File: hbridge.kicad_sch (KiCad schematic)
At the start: 25 parts, among them J11 Conn_01x06_Male, J12 Screw_Terminal_01x04, J21 Conn_01x03_Male, Q1 2N7000, Q11 2N7000, Q13 2N3904, Q14 2N3906, Q15 2N3904, Q16 2N3906, Q17 STP20NF06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

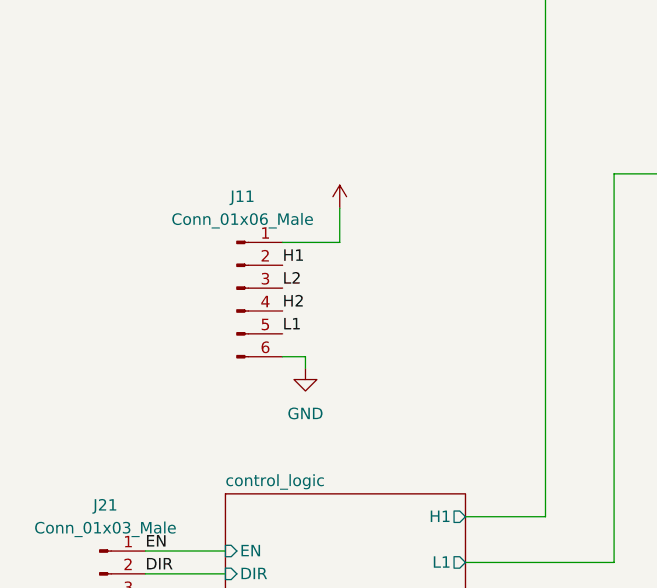
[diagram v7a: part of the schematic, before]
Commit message: Used internal layer to show redlines
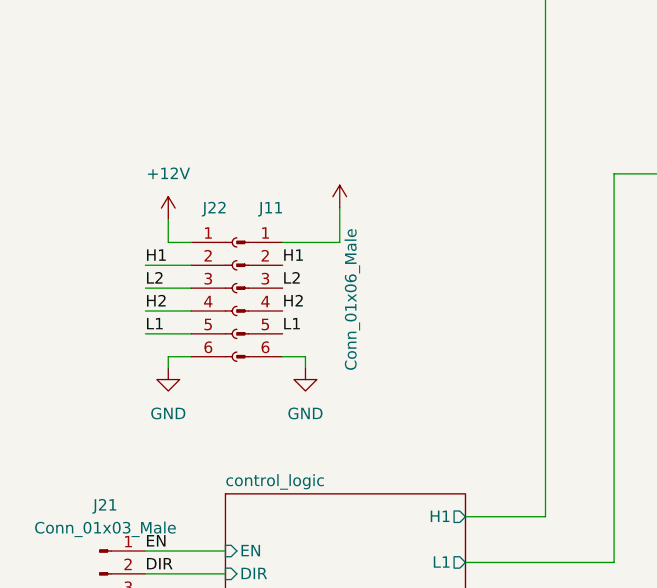
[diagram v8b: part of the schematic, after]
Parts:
- added J22: (no value), symbol Connector:Conn_01x06_Female
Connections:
- net +12V: now also J22.1 (Pin_1)
- net GND: now also J22.6 (Pin_6)
- net H1: now also J22.2 (Pin_2)
- net H2: now also J22.4 (Pin_4)
- net L1: now also J22.5 (Pin_5)
- net L2: now also J22.3 (Pin_3)
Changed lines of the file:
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@@
+    (stroke (width 0) (type default) (color 0 0 0 0))
+  )
+  (wire (pts (xy 35.56 105.41) (xy 38.1 105.41))
     (stroke (width 0) (type default) (color 0 0 0 0))
   )
@@
     (stroke (width 0) (type default) (color 0 0 0 0))
   )
+  (wire (pts (xy 33.02 100.33) (xy 38.1 100.33))
+    (stroke (width 0) (type default) (color 0 0 0 0))
+  )
   (wire (pts (xy 81.28 138.43) (xy 86.36 138.43))
     (stroke (width 0) (type default) (color 0 0 0 0))
@@
     (stroke (width 0) (type default) (color 0 0 0 0))
   )
+  (wire (pts (xy 35.56 106.68) (xy 35.56 105.41))
+    (stroke (width 0) (type default) (color 0 0 0 0))
+  )
   (wire (pts (xy 138.43 39.37) (xy 138.43 48.26))
     (stroke (width 0) (type default) (color 0 0 0 0))
@@
     (stroke (width 0) (type default) (color 0 0 0 0))
   )
+  (wire (pts (xy 35.56 92.71) (xy 38.1 92.71))
+    (stroke (width 0) (type default) (color 0 0 0 0))
+  )
   (wire (pts (xy 125.73 124.46) (xy 125.73 142.24))
     (stroke (width 0) (type default) (color 0 0 0 0))
@@
     (stroke (width 0) (type default) (color 0 0 0 0))
   )
+  (wire (pts (xy 33.02 97.79) (xy 38.1 97.79))
+    (stroke (width 0) (type default) (color 0 0 0 0))
+  )
   (wire (pts (xy 114.3 115.57) (xy 114.3 121.92))
     (stroke (width 0) (type default) (color 0 0 0 0))
@@
     (stroke (width 0) (type default) (color 0 0 0 0))
   )
+  (wire (pts (xy 35.56 90.17) (xy 35.56 92.71))
+    (stroke (width 0) (type default) (color 0 0 0 0))
+  )
   (wire (pts (xy 181.61 125.73) (xy 190.5 125.73))
     (stroke (width 0) (type default) (color 0 0 0 0))
@@
     (stroke (width 0) (type default) (color 0 0 0 0))
   )
+  (wire (pts (xy 33.02 102.87) (xy 38.1 102.87))
+    (stroke (width 0) (type default) (color 0 0 0 0))
+  )
   (wire (pts (xy 96.52 36.83) (xy 92.71 36.83))
     (stroke (width 0) (type default) (color 0 0 0 0))
@@
   )
   (wire (pts (xy 114.3 36.83) (xy 114.3 43.18))
+    (stroke (width 0) (type default) (color 0 0 0 0))
+  )
+  (wire (pts (xy 33.02 95.25) (xy 38.1 95.25))
     (stroke (width 0) (type default) (color 0 0 0 0))
   )
@@
     (effects (font (size 1.27 1.27)) (justify left bottom))
   )
+  (label "L1" (at 33.02 102.87 0)
+    (effects (font (size 1.27 1.27)) (justify left bottom))
+  )
   (label "OUT1" (at 153.67 63.5 0)
     (effects (font (size 1.27 1.27)) (justify left bottom))
   )
+  (label "L2" (at 33.02 97.79 0)
+    (effects (font (size 1.27 1.27)) (justify left bottom))
+  )
   (label "boot1" (at 116.84 36.83 0)
     (effects (font (size 1.27 1.27)) (justify left bottom))
@@
     (effects (font (size 1.27 1.27)) (justify left bottom))
   )
+  (label "H1" (at 33.02 95.25 0)
+    (effects (font (size 1.27 1.27)) (justify left bottom))
+  )
+  (label "H2" (at 33.02 100.33 0)
+    (effects (font (size 1.27 1.27)) (justify left bottom))
+  )
   (label "DIR" (at 33.02 129.54 0)
     (effects (font (size 1.27 1.27)) (justify left bottom))
@@
     )
     (property "Datasheet" "" (id 3) (at 92.71 114.3 0)
+      (effects (font (size 1.27 1.27)) hide)
+    )
+    (pin "1")
+  )
+  (symbol (lib_id "power:GND") (at 35.56 106.68 0) (unit 1)
+    (in_bom yes) (on_board yes) (fields_autoplaced)
+    (property "Reference" "#PWR0106" (id 0) (at 35.56 113.03 0)
+      (effects (font (size 1.27 1.27)) hide)
+    )
+    (property "Value" "GND" (id 1) (at 35.56 111.76 0))
+    (property "Footprint" "" (id 2) (at 35.56 106.68 0)
+      (effects (font (size 1.27 1.27)) hide)
+    )
+    (property "Datasheet" "" (id 3) (at 35.56 106.68 0)
       (effects (font (size 1.27 1.27)) hide)
     )
@@
     (pin "1")
   )
+  (symbol (lib_id "power:+12V") (at 35.56 90.17 0) (unit 1)
+    (in_bom yes) (on_board yes) (fields_autoplaced)
+    (property "Reference" "#PWR0107" (id 0) (at 35.56 93.98 0)
+      (effects (font (size 1.27 1.27)) hide)
+    )
+    (property "Value" "+12V" (id 1) (at 35.56 85.09 0))
+    (property "Footprint" "" (id 2) (at 35.56 90.17 0)
+      (effects (font (size 1.27 1.27)) hide)
+    )
+    (property "Datasheet" "" (id 3) (at 35.56 90.17 0)
+      (effects (font (size 1.27 1.27)) hide)
+    )
+    (pin "1")
+  )
   (symbol (lib_id "power:GND") (at 93.98 64.77 0) (unit 1)
     (in_bom yes) (on_board yes)
@@
     (pin "2")
   )
+  (symbol (lib_id "Connector:Conn_01x06_Female") (at 43.18 97.79 0) (unit 1)
+    (in_bom yes) (on_board yes)
+    (property "Reference" "J22" (id 0) (at 39.37 88.9 0)
+      (effects (font (size 1.27 1.27)) (justify left))
+    )
+    (property "Value" "" (id 1) (at 30.48 109.22 90)
+      (effects (font (size 1.27 1.27)) (justify left))
+    )
+    (property "Footprint" "" (id 2) (at 43.18 97.79 0)
+      (effects (font (size 1.27 1.27)) hide)
+    )
+    (property "Datasheet" "~" (id 3) (at 43.18 97.79 0)
+      (effects (font (size 1.27 1.27)) hide)
+    )
+    (pin "1")
+    (pin "2")
+    (pin "3")
+    (pin "4")
+    (pin "5")
+    (pin "6")
+  )
   (symbol (lib_id "power:GND") (at 50.8 106.68 0) (unit 1)
     (in_bom yes) (on_board yes) (fields_autoplaced)
@@
   )
   (symbol (lib_id "Connector:Conn_01x06_Male") (at 43.18 97.79 0) (unit 1)
-    (in_bom yes) (on_board yes) (fields_autoplaced)
-    (property "Reference" "J11" (id 0) (at 43.815 87.63 0))
-    (property "Value" "Conn_01x06_Male" (id 1) (at 43.815 90.17 0))
+    (in_bom yes) (on_board yes)
+    (property "Reference" "J11" (id 0) (at 46.99 88.9 0))
+    (property "Value" "Conn_01x06_Male" (id 1) (at 55.88 99.06 90))
     (property "Footprint" "Connector_PinHeader_2.54mm:PinHeader_1x06_P2.54mm_Vertical" (id 2) (at 43.18 97.79 0)
       (effects (font (size 1.27 1.27)) hide)
@@
       (reference "#PWR0105") (unit 1) (value "GND") (footprint "")
     )
+    (path "/03fc48c3-f1a0-4bb4-a2e5-dab73be4390e"
+      (reference "#PWR0106") (unit 1) (value "GND") (footprint "")
+    )
+    (path "/4a04e81e-870b-4066-97ff-3ebdbee2273b"
+      (reference "#PWR0107") (unit 1) (value "+12V") (footprint "")
+    )
     (path "/60edc9be-ffd4-4131-94ec-c92d31cecaae"
       (reference "C1") (unit 1) (value "1u") (footprint "Capacitor_SMD:C_0603_1608Metric")
@@
       (reference "J21") (unit 1) (value "Conn_01x03_Male") (footprint "Connector_PinHeader_2.54mm:PinHeader_1x03_P2.54mm_Vertical")
     )
+    (path "/af55655d-3b98-4345-bbcc-9b49a3ce693b"
+      (reference "J22") (unit 1) (value "Conn_01x06_Female") (footprint "Connector_PinSocket_2.54mm:PinSocket_1x06_P2.54mm_Vertical")
+    )
     (path "/71c26256-e6eb-4879-abd2-a101b47248f7"
